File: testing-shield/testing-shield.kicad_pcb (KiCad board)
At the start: 2 copper layers, 79.5 x 58.4 mm, 32 parts, among them J1 I2C Grove, J2 I2C Socket, J3 I2C Header, J4 Side SPI, J5 ISP SPI, J6 UART Header, J7 UART Grove, SW1 UART, SW2 Side SPI, SW3 ISP SPI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

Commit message: testing-shield: Fix R-2R DAC resistor values
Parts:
- R1, R2, R4, R6, R8: value 200R -> 20K
- R3, R5, R7: value 100R -> 10K
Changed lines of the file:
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@@
     (pad "4" thru_hole circle (at 3 0 270) (size 1.524 1.524) (drill 0.762) (layers "*.Cu" "*.Mask")
       (net 1 "GND") (pinfunction "Pin_4") (pintype "passive"))
-    (model "${KIPRJMOD}/grove.stp"
-      (offset (xyz -5 -3 0))
-      (scale (xyz 1 1 1))
-      (rotate (xyz -90 0 0))
-    )
   )
   (footprint "Package_DIP:DIP-16_W7.62mm" (layer "F.Cu")
@@
     (pad "4" thru_hole circle (at 3 0 90) (size 1.524 1.524) (drill 0.762) (layers "*.Cu" "*.Mask")
       (net 1 "GND") (pinfunction "Pin_4") (pintype "passive"))
-    (model "${KIPRJMOD}/grove.stp"
-      (offset (xyz -5 -3 0.5))
-      (scale (xyz 1 1 1))
-      (rotate (xyz -90 0 0))
-    )
   )
   (footprint "Button_Switch_THT:SW_DIP_SPSTx01_Slide_9.78x4.72mm_W7.62mm_P2.54mm" (layer "F.Cu")
@@
     (model "${KICAD6_3DMODEL_DIR}/Connector_PinHeader_2.54mm.3dshapes/PinHeader_1x03_P2.54mm_Vertical.wrl"
       (offset (xyz 0 0 0))
-      (scale (xyz 1 1 1))
-      (rotate (xyz 0 0 0))
-    )
-    (model "${KIPRJMOD}/jumper.stp"
-      (offset (xyz 0 -1.27 0))
       (scale (xyz 1 1 1))
       (rotate (xyz 0 0 0))
@@
         (effects (font (size 1 1) (thickness 0.15)) (justify mirror))
     )
-    (fp_text value "200R" (at 0 -1.65 -360) (layer "B.Fab") hide
+    (fp_text value "20K" (at 0 -1.65 -360) (layer "B.Fab") hide
         (effects (font (size 1 1) (thickness 0.15)) (justify mirror))
     )
@@
     (fp_line (start 1 0.625) (end 1 -0.625)
       (stroke (width 0.1) (type solid)) (layer "B.Fab"))
-    (pad "1" smd roundrect (at -0.9125 0) (size 1.025 1.4) (layers "B.Cu" "B.Paste" "B.Mask") (roundrect_rratio 0.243902)
+    (pad "1" smd roundrect (at -0.9125 0) (size 1.025 1.4) (layers "B.Cu" "B.Paste" "B.Mask") (roundrect_rratio 0.243902439)
       (net 8 "Net-(R3-Pad2)") (pintype "passive"))
-    (pad "2" smd roundrect (at 0.9125 0) (size 1.025 1.4) (layers "B.Cu" "B.Paste" "B.Mask") (roundrect_rratio 0.243902)
+    (pad "2" smd roundrect (at 0.9125 0) (size 1.025 1.4) (layers "B.Cu" "B.Paste" "B.Mask") (roundrect_rratio 0.243902439)
       (net 11 "/R-2R_2") (pintype "passive"))
     (model "${KICAD6_3DMODEL_DIR}/Resistor_SMD.3dshapes/R_0805_2012Metric.wrl"
@@
         (effects (font (size 1 1) (thickness 0.15)) (justify mirror))
     )
-    (fp_text value "100R" (at 0 -1.65 90) (layer "B.Fab") hide
+    (fp_text value "10K" (at 0 -1.65 90) (layer "B.Fab") hide
         (effects (font (size 1 1) (thickness 0.15)) (justify mirror))
     )
@@
     (fp_line (start 1 0.625) (end 1 -0.625)
       (stroke (width 0.1) (type solid)) (layer "B.Fab"))
-    (pad "1" smd roundrect (at -0.9125 0 90) (size 1.025 1.4) (layers "B.Cu" "B.Paste" "B.Mask") (roundrect_rratio 0.243902)
+    (pad "1" smd roundrect (at -0.9125 0 90) (size 1.025 1.4) (layers "B.Cu" "B.Paste" "B.Mask") (roundrect_rratio 0.243902439)
       (net 6 "Net-(R1-Pad2)") (pintype "passive"))
-    (pad "2" smd roundrect (at 0.9125 0 90) (size 1.025 1.4) (layers "B.Cu" "B.Paste" "B.Mask") (roundrect_rratio 0.243902)
+    (pad "2" smd roundrect (at 0.9125 0 90) (size 1.025 1.4) (layers "B.Cu" "B.Paste" "B.Mask") (roundrect_rratio 0.243902439)
       (net 8 "Net-(R3-Pad2)") (pintype "passive"))
     (model "${KICAD6_3DMODEL_DIR}/Resistor_SMD.3dshapes/R_0805_2012Metric.wrl"
@@
         (effects (font (size 1 1) (thickness 0.15)) (justify mirror))
     )
-    (fp_text value "200R" (at 0 -1.65 90) (layer "B.Fab") hide
+    (fp_text value "20K" (at 0 -1.65 90) (layer "B.Fab") hide
         (effects (font (size 1 1) (thickness 0.15)) (justify mirror))
     )
@@
     (fp_line (start 1 0.625) (end 1 -0.625)
       (stroke (width 0.1) (type solid)) (layer "B.Fab"))
-    (pad "1" smd roundrect (at -0.9125 0 90) (size 1.025 1.4) (layers "B.Cu" "B.Paste" "B.Mask") (roundrect_rratio 0.243902)
+    (pad "1" smd roundrect (at -0.9125 0 90) (size 1.025 1.4) (layers "B.Cu" "B.Paste" "B.Mask") (roundrect_rratio 0.243902439)
       (net 1 "GND") (pintype "passive"))
-    (pad "2" smd roundrect (at 0.9125 0 90) (size 1.025 1.4) (layers "B.Cu" "B.Paste" "B.Mask") (roundrect_rratio 0.243902)
+    (pad "2" smd roundrect (at 0.9125 0 90) (size 1.025 1.4) (layers "B.Cu" "B.Paste" "B.Mask") (roundrect_rratio 0.243902439)
       (net 6 "Net-(R1-Pad2)") (pintype "passive"))
     (model "${KICAD6_3DMODEL_DIR}/Resistor_SMD.3dshapes/R_0805_2012Metric.wrl"
@@
         (effects (font (size 1 1) (thickness 0.15)) (justify mirror))
     )
-    (fp_text value "200R" (at 0 -1.65 -360) (layer "B.Fab") hide
+    (fp_text value "20K" (at 0 -1.65 -360) (layer "B.Fab") hide
         (effects (font (size 1 1) (thickness 0.15)) (justify mirror))
     )
@@
     (fp_line (start 1 0.625) (end 1 -0.625)
       (stroke (width 0.1) (type solid)) (layer "B.Fab"))
-    (pad "1" smd roundrect (at -0.9125 0) (size 1.025 1.4) (layers "B.Cu" "B.Paste" "B.Mask") (roundrect_rratio 0.243902)
+    (pad "1" smd roundrect (at -0.9125 0) (size 1.025 1.4) (layers "B.Cu" "B.Paste" "B.Mask") (roundrect_rratio 0.243902439)
       (net 10 "Net-(R5-Pad2)") (pintype "passive"))
-    (pad "2" smd roundrect (at 0.9125 0) (size 1.025 1.4) (layers "B.Cu" "B.Paste" "B.Mask") (roundrect_rratio 0.243902)
+    (pad "2" smd roundrect (at 0.9125 0) (size 1.025 1.4) (layers "B.Cu" "B.Paste" "B.Mask") (roundrect_rratio 0.243902439)
       (net 13 "/R-2R_1") (pintype "passive"))
     (model "${KICAD6_3DMODEL_DIR}/Resistor_SMD.3dshapes/R_0805_2012Metric.wrl"
@@
         (effects (font (size 1 1) (thickness 0.15)) (justify mirror))
     )
-    (fp_text value "100R" (at 0 -1.65 90) (layer "B.Fab") hide
+    (fp_text value "10K" (at 0 -1.65 90) (layer "B.Fab") hide
         (effects (font (size 1 1) (thickness 0.15)) (justify mirror))
     )
@@
     (fp_line (start 1 0.625) (end 1 -0.625)
       (stroke (width 0.1) (type solid)) (layer "B.Fab"))
-    (pad "1" smd roundrect (at -0.9125 0 90) (size 1.025 1.4) (layers "B.Cu" "B.Paste" "B.Mask") (roundrect_rratio 0.243902)
+    (pad "1" smd roundrect (at -0.9125 0 90) (size 1.025 1.4) (layers "B.Cu" "B.Paste" "B.Mask") (roundrect_rratio 0.243902439)
       (net 8 "Net-(R3-Pad2)") (pintype "passive"))
-    (pad "2" smd roundrect (at 0.9125 0 90) (size 1.025 1.4) (layers "B.Cu" "B.Paste" "B.Mask") (roundrect_rratio 0.243902)
+    (pad "2" smd roundrect (at 0.9125 0 90) (size 1.025 1.4) (layers "B.Cu" "B.Paste" "B.Mask") (roundrect_rratio 0.243902439)
       (net 10 "Net-(R5-Pad2)") (pintype "passive"))
     (model "${KICAD6_3DMODEL_DIR}/Resistor_SMD.3dshapes/R_0805_2012Metric.wrl"
@@
         (effects (font (size 1 1) (thickness 0.15)) (justify mirror))
     )
-    (fp_text value "200R" (at 0 -1.65 -360) (layer "B.Fab") hide
+    (fp_text value "20K" (at 0 -1.65 -360) (layer "B.Fab") hide
         (effects (font (size 1 1) (thickness 0.15)) (justify mirror))
     )
@@
     (fp_line (start 1 0.625) (end 1 -0.625)
       (stroke (width 0.1) (type solid)) (layer "B.Fab"))
-    (pad "1" smd roundrect (at -0.9125 0) (size 1.025 1.4) (layers "B.Cu" "B.Paste" "B.Mask") (roundrect_rratio 0.243902)
+    (pad "1" smd roundrect (at -0.9125 0) (size 1.025 1.4) (layers "B.Cu" "B.Paste" "B.Mask") (roundrect_rratio 0.243902439)
       (net 12 "/A0") (pintype "passive"))
-    (pad "2" smd roundrect (at 0.9125 0) (size 1.025 1.4) (layers "B.Cu" "B.Paste" "B.Mask") (roundrect_rratio 0.243902)
+    (pad "2" smd roundrect (at 0.9125 0) (size 1.025 1.4) (layers "B.Cu" "B.Paste" "B.Mask") (roundrect_rratio 0.243902439)
       (net 14 "/R-2R_0") (pintype "passive"))
     (model "${KICAD6_3DMODEL_DIR}/Resistor_SMD.3dshapes/R_0805_2012Metric.wrl"
@@
         (effects (font (size 1 1) (thickness 0.15)) (justify mirror))
     )
-    (fp_text value "200R" (at 0 -1.65 -360) (layer "B.Fab") hide
+    (fp_text value "20K" (at 0 -1.65 -360) (layer "B.Fab") hide
         (effects (font (size 1 1) (thickness 0.15)) (justify mirror))
     )
@@
     (fp_line (start 1 0.625) (end 1 -0.625)
       (stroke (width 0.1) (type solid)) (layer "B.Fab"))
-    (pad "1" smd roundrect (at -0.9125 0) (size 1.025 1.4) (layers "B.Cu" "B.Paste" "B.Mask") (roundrect_rratio 0.243902)
+    (pad "1" smd roundrect (at -0.9125 0) (size 1.025 1.4) (layers "B.Cu" "B.Paste" "B.Mask") (roundrect_rratio 0.243902439)
       (net 6 "Net-(R1-Pad2)") (pintype "passive"))
-    (pad "2" smd roundrect (at 0.9125 0) (size 1.025 1.4) (layers "B.Cu" "B.Paste" "B.Mask") (roundrect_rratio 0.243902)
+    (pad "2" smd roundrect (at 0.9125 0) (size 1.025 1.4) (layers "B.Cu" "B.Paste" "B.Mask") (roundrect_rratio 0.243902439)
       (net 9 "/R-2R_3") (pintype "passive"))
     (model "${KICAD6_3DMODEL_DIR}/Resistor_SMD.3dshapes/R_0805_2012Metric.wrl"
@@
         (effects (font (size 1 1) (thickness 0.15)) (justify mirror))
     )
-    (fp_text value "100R" (at 0 -1.65 90) (layer "B.Fab") hide
+    (fp_text value "10K" (at 0 -1.65 90) (layer "B.Fab") hide
         (effects (font (size 1 1) (thickness 0.15)) (justify mirror))
     )
@@
     (fp_line (start 1 0.625) (end 1 -0.625)
       (stroke (width 0.1) (type solid)) (layer "B.Fab"))
-    (pad "1" smd roundrect (at -0.9125 0 90) (size 1.025 1.4) (layers "B.Cu" "B.Paste" "B.Mask") (roundrect_rratio 0.243902)
+    (pad "1" smd roundrect (at -0.9125 0 90) (size 1.025 1.4) (layers "B.Cu" "B.Paste" "B.Mask") (roundrect_rratio 0.243902439)
       (net 10 "Net-(R5-Pad2)") (pintype "passive"))
-    (pad "2" smd roundrect (at 0.9125 0 90) (size 1.025 1.4) (layers "B.Cu" "B.Paste" "B.Mask") (roundrect_rratio 0.243902)
+    (pad "2" smd roundrect (at 0.9125 0 90) (size 1.025 1.4) (layers "B.Cu" "B.Paste" "B.Mask") (roundrect_rratio 0.243902439)
       (net 12 "/A0") (pintype "passive"))
     (model "${KICAD6_3DMODEL_DIR}/Resistor_SMD.3dshapes/R_0805_2012Metric.wrl"

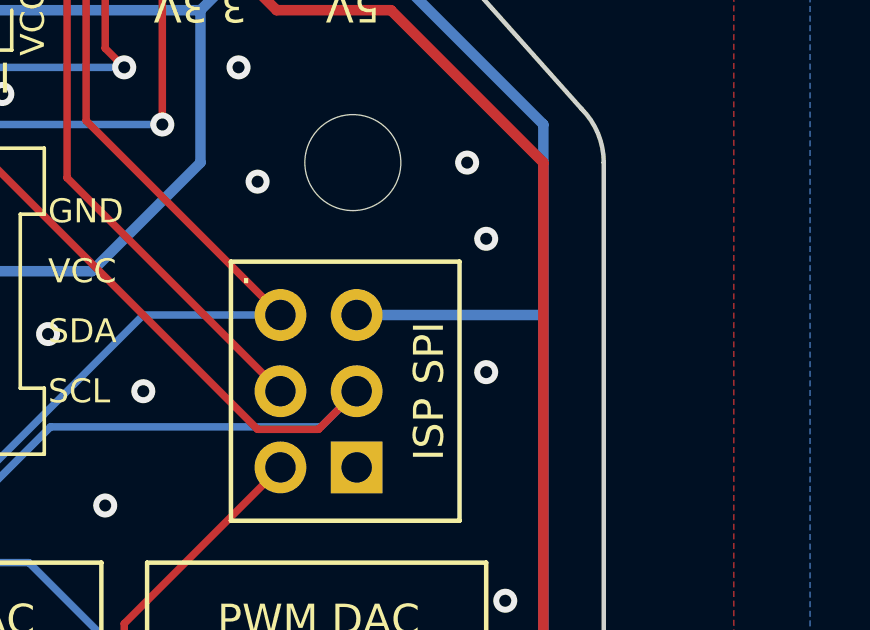
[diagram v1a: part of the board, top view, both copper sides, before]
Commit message: testing-shield: do not connect to 5V pin of ISP
Some boards (e.g. the Seeeduino) do not have 5V but VCC there.
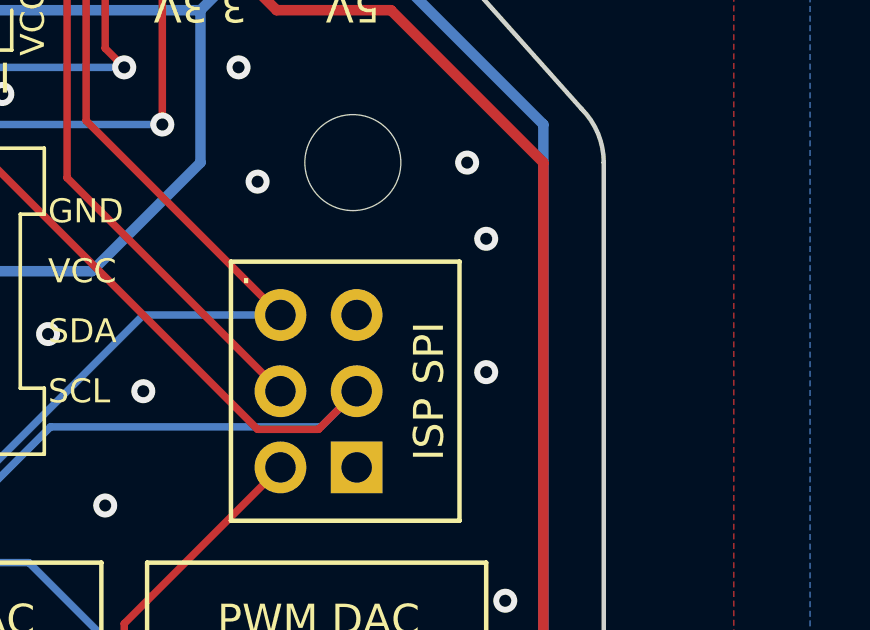
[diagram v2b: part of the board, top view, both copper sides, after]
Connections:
- XA1 pad 5V2: +5V -> unconnected-(XA1-SPI_5V-Pad5V2)
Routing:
- net +5V: track 83.7 -> 77.4 mm
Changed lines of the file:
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@@
   (net 42 "unconnected-(XA1-PadVIN)")
   (net 43 "/A3")
+  (net 44 "unconnected-(XA1-SPI_5V-Pad5V2)")
   (footprint "boards:grove_uart" (layer "F.Cu")
     (at 136.525 68.12 -90)
@@
       (net 31 "+5V") (pinfunction "5V") (pintype "power_in"))
     (pad "5V2" thru_hole oval locked (at 66.167 -30.48) (size 1.7272 1.7272) (drill 1.016) (layers "*.Cu" "*.Mask")
-      (net 31 "+5V") (pinfunction "SPI_5V") (pintype "power_in"))
+      (net 44 "unconnected-(XA1-SPI_5V-Pad5V2)") (pinfunction "SPI_5V") (pintype "power_in+no_connect"))
     (pad "A0" thru_hole oval locked (at 50.8 -2.54) (size 1.7272 1.7272) (drill 1.016) (layers "*.Cu" "*.Mask")
       (net 12 "/A0") (pinfunction "A0") (pintype "bidirectional"))
@@
   (segment (start 129.54 96.52) (end 132.08 99.06) (width 0.35) (layer "B.Cu") (net 31))
   (segment (start 163.83 68.58) (end 163.83 92.71) (width 0.35) (layer "B.Cu") (net 31))
-  (segment (start 157.607 68.58) (end 163.83 68.58) (width 0.35) (layer "B.Cu") (net 31))
   (segment (start 163.83 92.71) (end 157.48 99.06) (width 0.35) (layer "B.Cu") (net 31))
   (segment (start 96.035 51.435) (end 89.535 51.435) (width 0.25) (layer "F.Cu") (net 32))

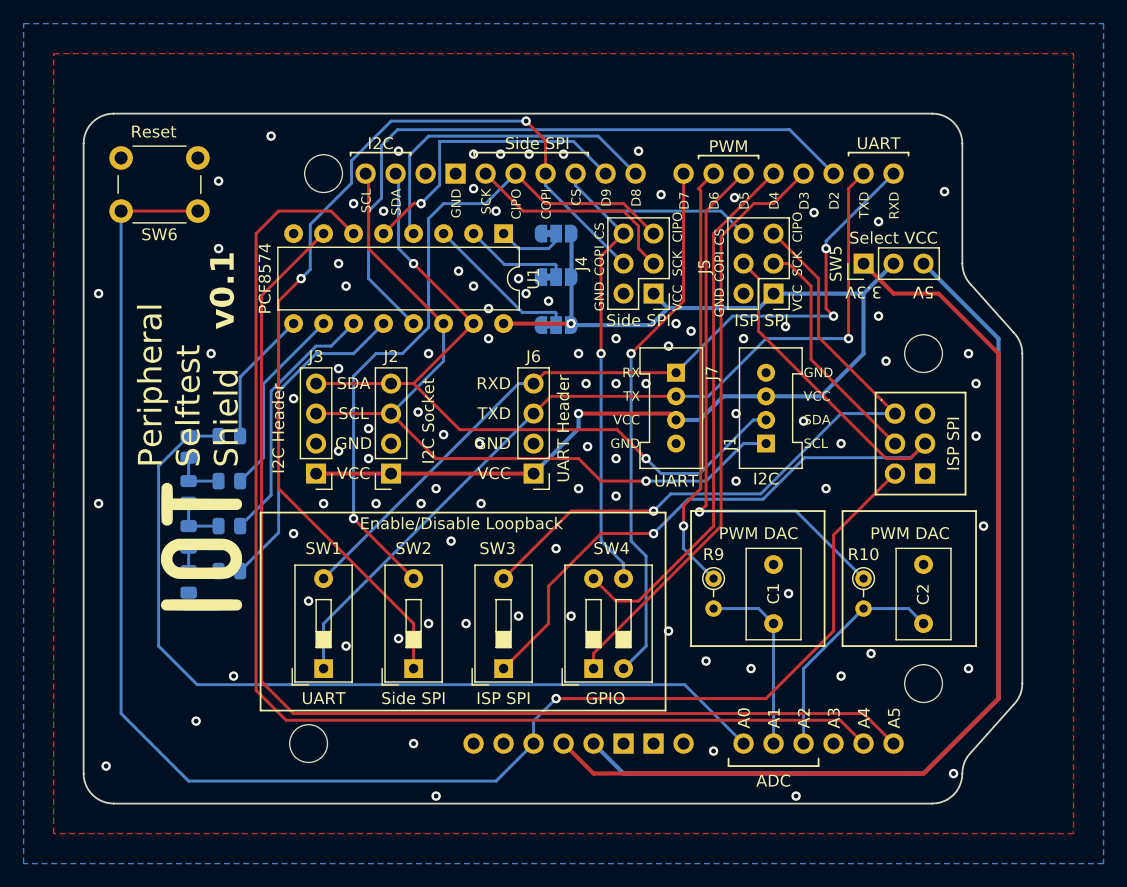
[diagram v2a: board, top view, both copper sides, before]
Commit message: testing-shield: connect SCK lines to GPIO extender
This allows reading the SPI clock polarity when the SPI clock is
idle.
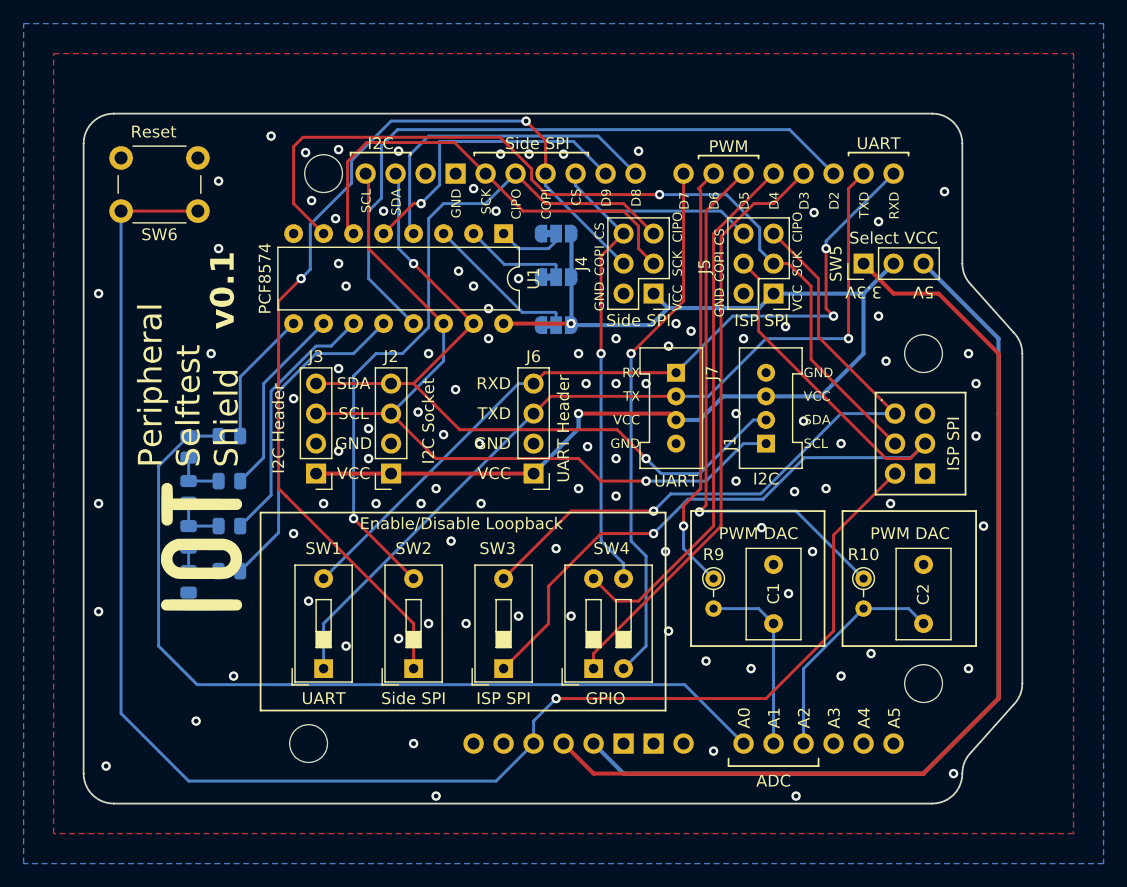
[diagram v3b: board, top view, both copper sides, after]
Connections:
- U1 pad 6: /A4 -> /SCK_0
- U1 pad 7: /A5 -> /SCK_1
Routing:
- net /A4: track 101.8 -> 0.00 mm
- net /A5: track 95.8 -> 0.00 mm
- net /SCK_1: track 20.2 -> 75.7 mm, vias 0 -> 1
- net /SCK_0: track 18.5 -> 38.2 mm
- net GND: vias 94 -> 99
